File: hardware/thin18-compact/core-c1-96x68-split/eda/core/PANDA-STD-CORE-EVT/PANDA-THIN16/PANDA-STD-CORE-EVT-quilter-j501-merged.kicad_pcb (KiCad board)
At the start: 4 copper layers, 96 x 68 mm, 148 parts, among them J201 USB4500-03-0-A, J301 DF58-2P-1.2V(21), J302 SM03B-SRSS-TB NTC, J501 104031-0811 / microSD, J502 SM02B-SRSS-TB, J503 TC2030-IDC-NL / DEBUG, J601 DF40C-60DS-0.4V(58), J803 FH34SRJ-6S-0.5SH(50), J804 FH34SRJ-6S-0.5SH(50), SW201 SKSCLCE010, SW202 SKSCLCE010, U302 RV-3028-C7, U402 TPS22916CYFPT, U403 TPS22916CYFPT, U404 TPS22916CYFPT, U405 TPS22916CYFPT, U501 ESP32-S3-WROOM-1U-N16R8, U503 QMI8658A, U601 XL9535, U901 SGM41513YTQF24G/TR, U902 SGM62125AXG/TR, U903 CW2217BAAD, U904 NS4168, U905 SGM37601YTRL20G/TR

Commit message: hw: correct prototype footprints and prepare Split-C1 JLC CAM handoff
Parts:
- C301: footprint Capacitor_SMD:C_1210_3225Metric -> panda-standard:CPH3225A_Polarized_Derived
- L402: footprint panda-standard:L402_2U2_ENVELOPE -> panda-standard:XGL4015_Coilcraft

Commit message: hw: apply reviewed domestic ECOs and gate incomplete Split-C1 orders
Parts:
- added C516: 1u / U403 VOUT, Capacitor_SMD:C_0603_1608Metric, B.Cu at (37.9, 15.9)
- J601: value DF40C-60DS-0.4V(58) -> HC-PBB40C-60DS-0.4V-1.5-02; footprint Connector_Hirose_DF40:Hirose_DF40C-60DS-0.4V_2x30_P0.4mm -> panda-standard:HCTL_PBB40C_60DS_04V_15
- U402, U403, U404, U405: value TPS22916CYFPT -> SGM2578SDYG/TR; footprint panda-standard:TPS22916CYFPT_YFP0004 -> panda-standard:SGM2578SD_WLCSP_09x09_P05
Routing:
- net GND: track 718.0 -> 722.3 mm, vias 20 -> 21
- net 3V3_TOUCH_SW: track 9.48 -> 10.0 mm

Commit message: hw: apply domestic wire, FPC and inductor ECOs with replay guards
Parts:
- J302: value SM03B-SRSS-TB NTC -> HC-1.0-3PWT NTC; footprint Connector_JST:JST_SH_SM03B-SRSS-TB_1x03-1MP_P1.00mm_Horizontal -> panda-standard:HCTL_HC10_3PWT
- J502: value SM02B-SRSS-TB -> HC-1.0-2PWT BTL; footprint Connector_JST:JST_SH_SM02B-SRSS-TB_1x02-1MP_P1.00mm_Horizontal -> panda-standard:HCTL_HC10_2PWT
- J803, J804: value FH34SRJ-6S-0.5SH(50) -> X05A10H06G; footprint PandaDomestic:FH34SRJ-6S-0.5SH_50 -> panda-standard:XKB_X05A10H06G_A2
- L401: value 0.47uH / M0-PENDING -> 0.47uH / SGM62125; footprint panda-standard:L401_XFL4015_ENVELOPE -> panda-standard:Sunlord_MWSA0402_R47
- L402: value 2.2u / BQ buck -> 1uH / SGM41513 buck; footprint panda-standard:XGL4015_Coilcraft -> panda-standard:Sunlord_MWSA0402_1R0B01
- moved J803 2.50 mm to (6.35, 36.9), turned to 180 degrees
- moved J804 2.50 mm to (6.35, 43.0), turned to 180 degrees
- moved H804 1.00 mm to (3.00, 33.0)
- moved L402 0.55 mm to (40.7, 6.65), turned to 270 degrees
- moved C402 0.40 mm to (34.9, 4.96)
- moved R306 0.40 mm to (35.6, 9.25)
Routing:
- net VSYS_RAW: track 75.2 -> 77.4 mm
- net BAT_PACKP: track 60.0 -> 61.7 mm, vias 5 -> 6
- net GND: track 722.3 -> 723.4 mm
- net SGM41513_SW: track 5.51 -> 6.47 mm
- net BQ_TS: track 65.6 -> 66.4 mm

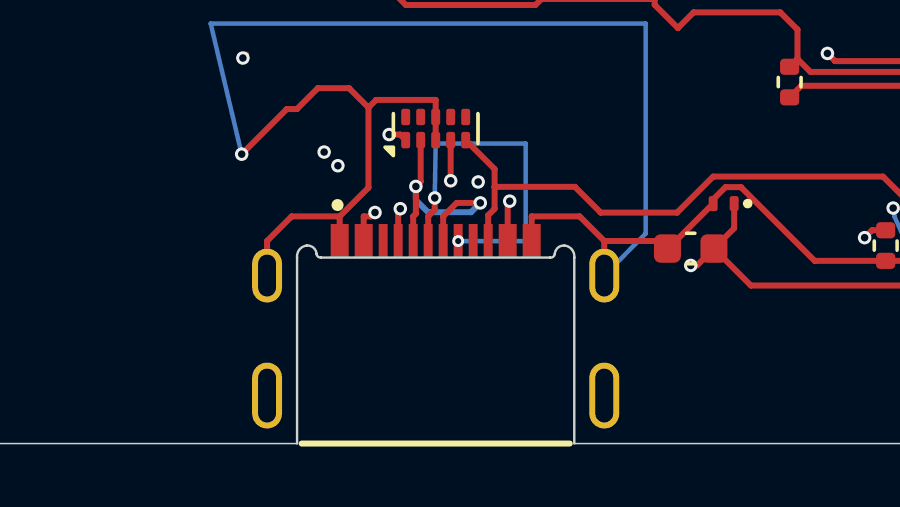
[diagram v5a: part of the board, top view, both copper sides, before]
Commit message: hw: replace USB-C with MUP and clear standard board-edge DFM
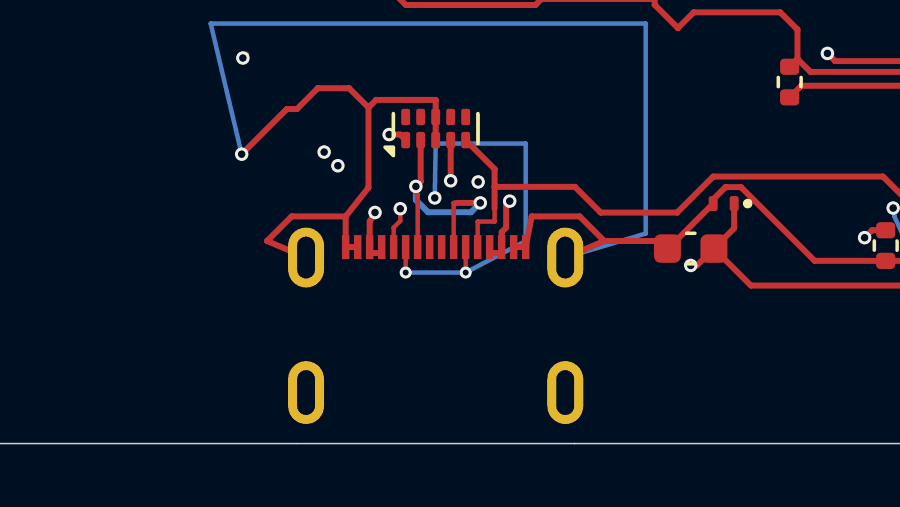
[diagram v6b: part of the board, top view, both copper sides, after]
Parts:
- J201: value USB4500-03-0-A -> U20405-01 USB2.0; footprint panda-layout:USB4500_08mm_MidMount_LayoutReview -> panda-standard:MUP_U20405_01_R4
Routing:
- net GND: track 723.4 -> 727.1 mm
- net USB_DM: track 41.6 -> 44.7 mm
- net USB_DP: track 50.2 -> 52.4 mm, vias 4 -> 5
- net VBUS_USB: track 99.8 -> 101.7 mm
- net USB_CC2: track 20.6 -> 21.3 mm

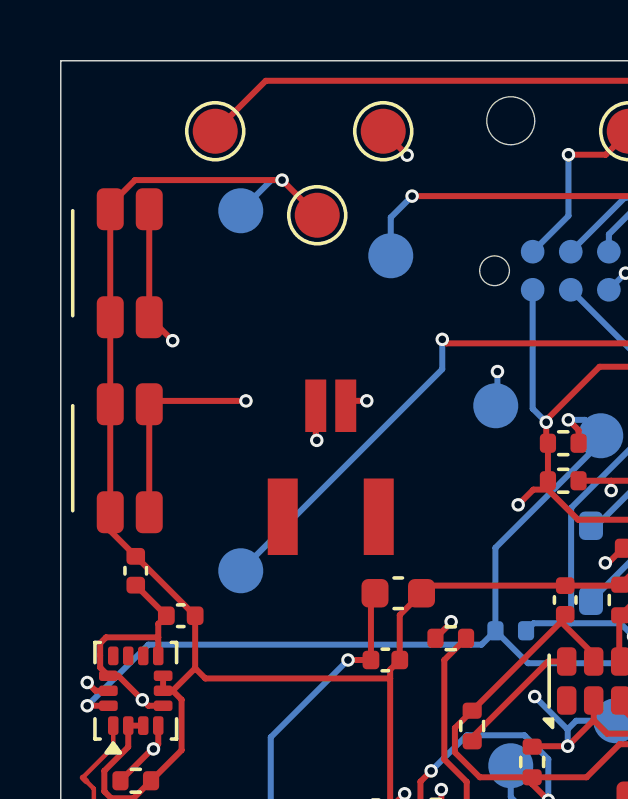
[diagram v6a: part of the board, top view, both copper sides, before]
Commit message: hw: replace side buttons with XKB A1 no-post switches
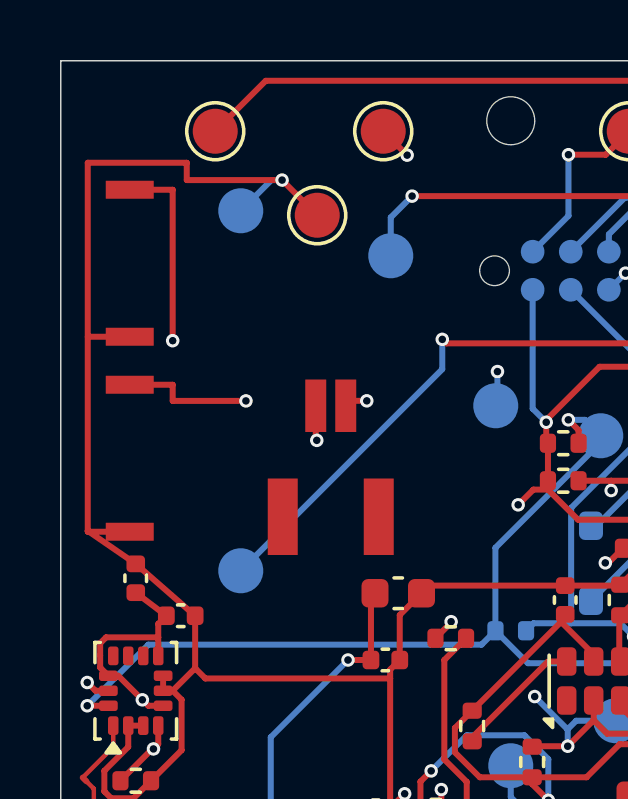
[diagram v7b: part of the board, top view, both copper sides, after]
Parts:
- SW201, SW202: value SKSCLCE010 -> TS-1186E-B-B; footprint panda-standard:SW_Alps_SKSCLCE010 -> panda-standard:XKB_TS1186E_BB_A1
- moved C504 0.25 mm to (2.50, 17.2)
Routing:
- net GND: track 727.1 -> 732.9 mm
- net BQ_QON: track 58.1 -> 55.7 mm
- net KEY_POWER_MCU: track 116.7 -> 118.5 mm

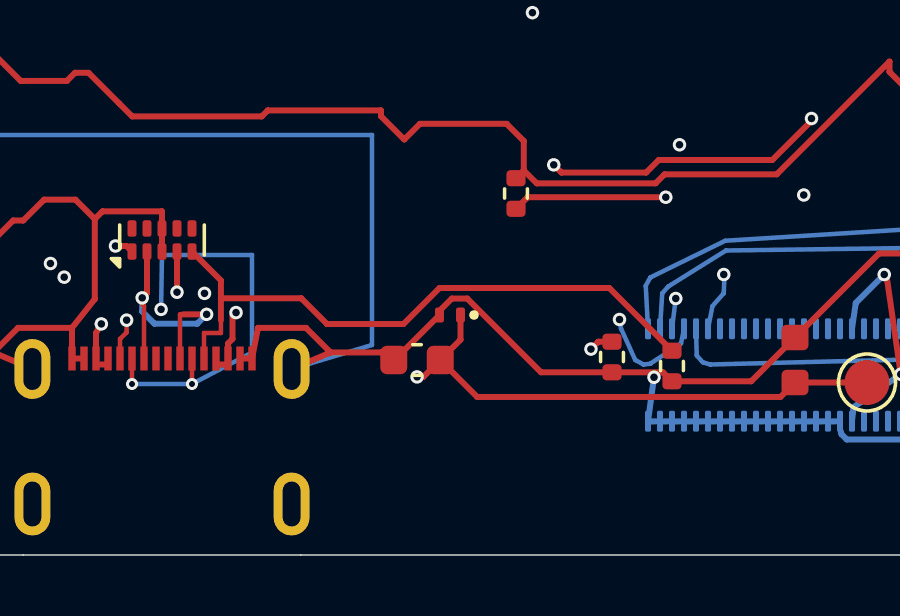
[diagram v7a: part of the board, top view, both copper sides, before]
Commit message: hw: replace Split-C1 VBUS TVS with polarized SGMICRO protection
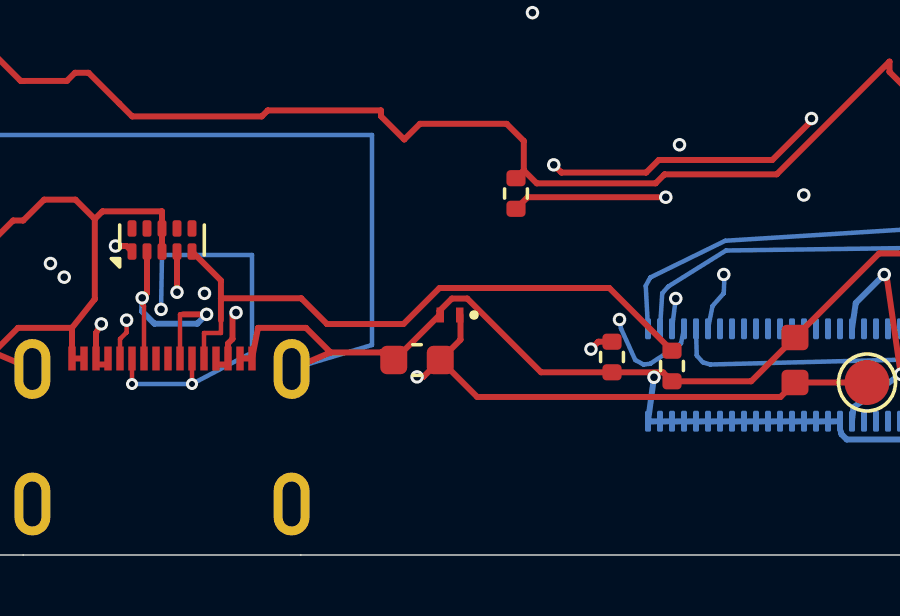
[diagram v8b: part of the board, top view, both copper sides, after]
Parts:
- D202: value TPD1E10B06DPYR -> SGM05HU1ALXUGY2G/TR; footprint Package_SON:Texas_DPY0002A_0.6x1mm_P0.65mm -> panda-standard:SGM05HU1AL_UTDFN_1006_2BL
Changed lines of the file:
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@@
 )
 	(footprint "Capacitor_SMD:C_0603_1608Metric" (locked yes) (layer "F.Cu") (at 74 53.75) (descr "Capacitor SMD 0603 (1608 Metric), square (rectangular) end terminal, IPC-7351 nominal, (Body size source: IPC-SM-782 page 76, https://www.pcb-3d.com/wordpress/wp-content/uploads/ipc-sm-782a_amendment_1_and_2.pdf)") (tags "capacitor") (property "Reference" "C510" (at 0 -1.43 180) (layer "F.Fab") (hide yes) (effects (font (size 1 1) (thickness 0.15)))) (property "Value" "1u / CHIP_PU" (at 0 1.43 180) (layer "F.Fab") (effects (font (size 1 1) (thickness 0.15)))) (property "Datasheet" "https://www.fhcomp.com/en/product_info/?prod_code=0603B105K250NT" (at 0 0 180) (layer "F.Fab") (hide yes) (effects (font (size 1.27 1.27)))) (property "Description" "FH 1uF 25V X7R +/-10% 0603 local input bypass for SGM2578SD. Application review in split-c1-domestic-eco.json; DC-bias remains qualification." (at 0 0 180) (layer "F.Fab") (hide yes) (effects (font (size 1.27 1.27)))) (property "KiLib_Generator" "SMD_2terminal_chip_molded" (at 0 0 180) (layer "F.SilkS") (hide yes) (effects (font (size 1 1) (thickness 0.15)))) (property "Manufacturer" "FH (Fenghua Advanced)" (at 0 0 0) (layer "F.Fab") (hide yes) (effects (font (size 1 1) (thickness 0.15)))) (property "MPN" "0603B105K250NT" (at 0 0 0) (layer "F.Fab") (hide yes) (effects (font (size 1 1) (thickness 0.15)))) (property "LCSC" "C59302" (at 0 0 0) (layer "F.Fab") (hide yes) (effects (font (size 1 1) (thickness 0.15)))) (property "ECO_ID" "THIN18-C4-FH-PASSIVE" (at 0 0 0) (layer "F.Fab") (hide yes) (effects (font (size 1 1) (thickness 0.15)))) (property "Qualification" "1uF ±10% 25V X7R 0603; same footprint; physical assembly/DC-bias qualification open" (at 0 0 0) (layer "F.Fab") (hide yes) (effects (font (size 1 1) (thickness 0.15)))) (attr smd) (duplicate_pad_numbers_are_jumpers no) (fp_line (start -0.14058 -0.51) (end 0.14058 -0.51) (stroke (width 0.12) (type solid)) (layer "F.SilkS")) (fp_line (start -0.14058 0.51) (end 0.14058 0.51) (stroke (width 0.12) (type solid)) (layer "F.SilkS")) (fp_rect (start -1.48 -0.73) (end 1.48 0.73) (stroke (width 0.05) (type solid)) (fill no) (layer "F.CrtYd")) (fp_rect (start -0.8 -0.4) (end 0.8 0.4) (stroke (width 0.1) (type solid)) (fill no) (layer "F.Fab")) (fp_text user "${REFERENCE}" (at 0 0 180) (layer "F.Fab") (effects (font (size 0.4 0.4) (thickness 0.06)))) (pad "1" smd roundrect (at -0.775 0) (size 0.9 0.95) (layers "F.Cu" "F.Mask" "F.Paste") (roundrect_rratio 0.25) (net "CHIP_PU")) (pad "2" smd roundrect (at 0.775 0) (size 0.9 0.95) (layers "F.Cu" "F.Mask" "F.Paste") (roundrect_rratio 0.25) (net "GND")) (embedded_fonts no) (model "${KICAD10_3DMODEL_DIR}/Capacitor_SMD.3dshapes/C_0603_1608Metric.step" (offset (xyz 0 0 0)) (scale (xyz 1 1 1)) (rotate (xyz 0 0 0))))
-	(footprint "Package_SON:Texas_DPY0002A_0.6x1mm_P0.65mm" (locked yes) (layer "F.Cu") (at 48.6 60 180) (descr "X1SON 2 pin 0.6x1mm 0.375mm height package, https://www.ti.com/lit/ml/mpss034c/mpss034c.pdf, https://www.ti.com/lit/ds/symlink/tpd6e05u06.pdf") (tags "X1SON") (property "Reference" "D202" (at 0 -1.25 180) (unlocked yes) (layer "F.SilkS") (hide yes) (effects (font (size 1 1) (thickness 0.15)))) (property "Value" "TPD1E10B06DPYR" (at 0 1.25 180) (unlocked yes) (layer "F.Fab") (effects (font (size 1 1) (thickness 0.15)))) (property "Datasheet" "https://www.ti.com/lit/ds/symlink/tpd1e10b06.pdf" (at 0 0 180) (unlocked yes) (layer "F.Fab") (hide yes) (effects (font (size 1.27 1.27) (thickness 0.15))))
-(property "LCSC" "C48260" (at 0 0 180) (unlocked yes) (layer "F.Fab") (hide yes) (effects (font (size 1.27 1.27) (thickness 0.15))))(property "Manufacturer" "Texas Instruments" (at 0 0 180) (layer "F.Fab") (hide yes) (effects (font (size 1 1))))(property "MPN" "TPD1E10B06DPYR" (at 0 0 180) (layer "F.Fab") (hide yes) (effects (font (size 1 1)))) (property "Description" "" (at 0 0 180) (unlocked yes) (layer "F.Fab") (hide yes) (effects (font (size 1.27 1.27) (thickness 0.15)))) (attr smd) (duplicate_pad_numbers_are_jumpers no) (fp_circle (center -0.8 0) (end -0.69 0) (stroke (width 0.1) (type solid)) (fill yes) (layer "F.SilkS")) (fp_rect (start -0.65 -0.45) (end 0.65 0.45) (stroke (width 0.05) (type solid)) (fill no) (layer "F.CrtYd")) (fp_line (start -0.2 0.3) (end -0.2 -0.3) (stroke (width 0.1) (type solid)) (layer "F.Fab")) (fp_line (start -0.3 0.3) (end -0.3 -0.3) (stroke (width 0.1) (type solid)) (layer "F.Fab")) (fp_line (start -0.4 0.3) (end -0.4 -0.3) (stroke (width 0.1) (type solid)) (layer "F.Fab")) (fp_rect (start -0.5 -0.3) (end 0.5 0.3) (stroke (width 0.1) (type solid)) (fill no) (layer "F.Fab")) (fp_text user "${REFERENCE}" (at 0 0 180) (layer "F.Fab") (effects (font (size 0.25 0.25) (thickness 0.04)))) (pad "1" smd roundrect (at -0.35 0 180) (size 0.3 0.5) (layers "F.Cu" "F.Mask" "F.Paste") (roundrect_rratio 0.25) (net "VBUS_USB")) (pad "2" smd roundrect (at 0.35 0 180) (size 0.3 0.5) (layers "F.Cu" "F.Mask" "F.Paste") (roundrect_rratio 0.25) (net "GND")) (embedded_fonts no) (model "${KICAD10_3DMODEL_DIR}/Package_SON.3dshapes/Texas_DPY0002A_0.6x1mm_P0.65mm.step" (offset (xyz 0 0 0)) (scale (xyz 1 1 1)) (rotate (xyz 0 0 0))))
+	(footprint "panda-standard:SGM05HU1AL_UTDFN_1006_2BL" (locked yes) (layer "F.Cu") (at 48.6 60 180) (descr "SGMICRO SGM05HU1ALXUGY2G/TR, August2024 Rev.A. Unidirectional5.5V VRWM;1=cathode/VBUS,2=anode/GND. Primary0.25x0.50mm lands at0.65mm pitch.5V USB sink only/no PD; board ESD, leakage and exact assembly supply pending.") (tags "SGMICRO VBUS unidirectional cathode-pin1 UTDFN1006") (property "Reference" "D202" (at 0 -1.25 180) (unlocked yes) (layer "F.SilkS") (hide yes) (effects (font (size 1 1) (thickness 0.15)))) (property "Value" "SGM05HU1ALXUGY2G/TR" (at 0 1.25 180) (unlocked yes) (layer "F.Fab") (effects (font (size 1 1) (thickness 0.15)))) (property "Datasheet" "https://www.sg-micro.com/rect/assets/eb558bde-b3be-44cb-ae7e-2a8337e06580/SGM05HU1AL.pdf" (at 0 0 180) (unlocked yes) (layer "F.Fab") (hide yes) (effects (font (size 1.27 1.27) (thickness 0.15))))
+(property "LCSC" "" (at 0 0 180) (unlocked yes) (layer "F.Fab") (hide yes) (effects (font (size 1.27 1.27) (thickness 0.15))))(property "Manufacturer" "SGMICRO" (at 0 0 180) (layer "F.Fab") (hide yes) (effects (font (size 1 1))))(property "MPN" "SGM05HU1ALXUGY2G/TR" (at 0 0 180) (layer "F.Fab") (hide yes) (effects (font (size 1 1)))) (property "Description" "SGMICRO SGM05HU1ALXUGY2G/TR, August2024 Rev.A. Unidirectional5.5V VRWM;1=cathode/VBUS,2=anode/GND. Primary0.25x0.50mm lands at0.65mm pitch.5V USB sink only/no PD; board ESD, leakage and exact assembly supply pending." (at 0 0 180) (unlocked yes) (layer "F.Fab") (hide yes) (effects (font (size 1.27 1.27) (thickness 0.15)))) (attr smd) (duplicate_pad_numbers_are_jumpers no)        (pad "1" smd rect (at -0.325 0 180) (size 0.25 0.50) (layers "F.Cu" "F.Mask" "F.Paste") (net "VBUS_USB")) (pad "2" smd rect (at 0.325 0 180) (size 0.25 0.50) (layers "F.Cu" "F.Mask" "F.Paste") (net "GND")) (embedded_fonts no)
+(fp_rect (start -0.525 -0.325) (end 0.525 0.325) (stroke (width 0.1) (type solid)) (fill no) (layer "F.Fab"))
+(fp_rect (start -0.75 -0.55) (end 0.75 0.55) (stroke (width 0.05) (type solid)) (fill no) (layer "F.CrtYd"))
+(fp_line (start -0.4 -0.3) (end -0.4 0.3) (stroke (width .1) (type solid)) (layer "F.Fab"))
+(fp_circle (center -.8 0) (end -.69 0) (stroke (width .1) (type solid)) (fill yes) (layer "F.SilkS"))
+)
 	(footprint "panda-standard:CW2217BAAD_DFN12_L4.0_W2.5_P0.4_EP" (locked yes) (layer "F.Cu")
  (at 42.6 32.65)
